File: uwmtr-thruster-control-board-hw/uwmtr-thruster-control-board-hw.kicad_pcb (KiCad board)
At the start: 4 copper layers, 40 x 49.2 mm, 16 parts, among them J1 Conn_01x13_Pin, J2 691137710003, J3 691137710002, U1 TI_MCF8316A

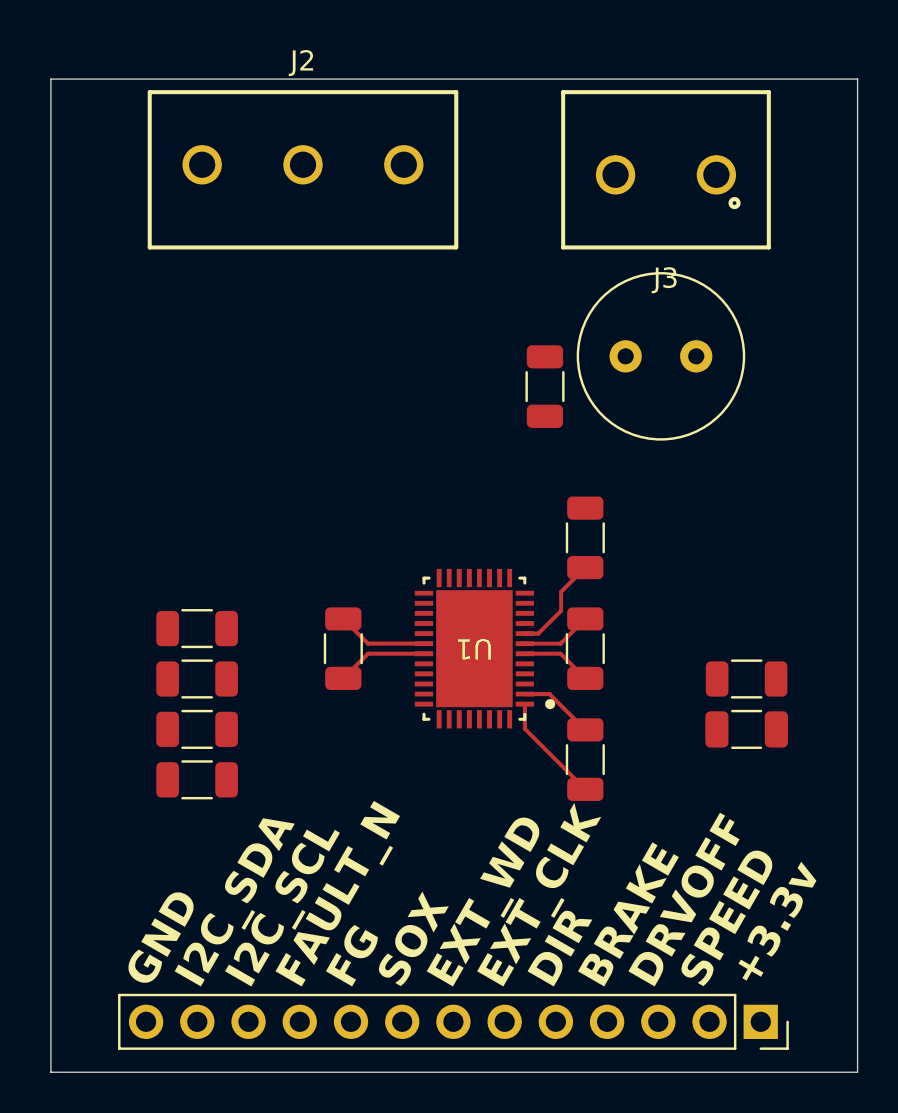
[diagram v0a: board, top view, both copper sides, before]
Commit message: Completing component placement for layout and replacing the resistor
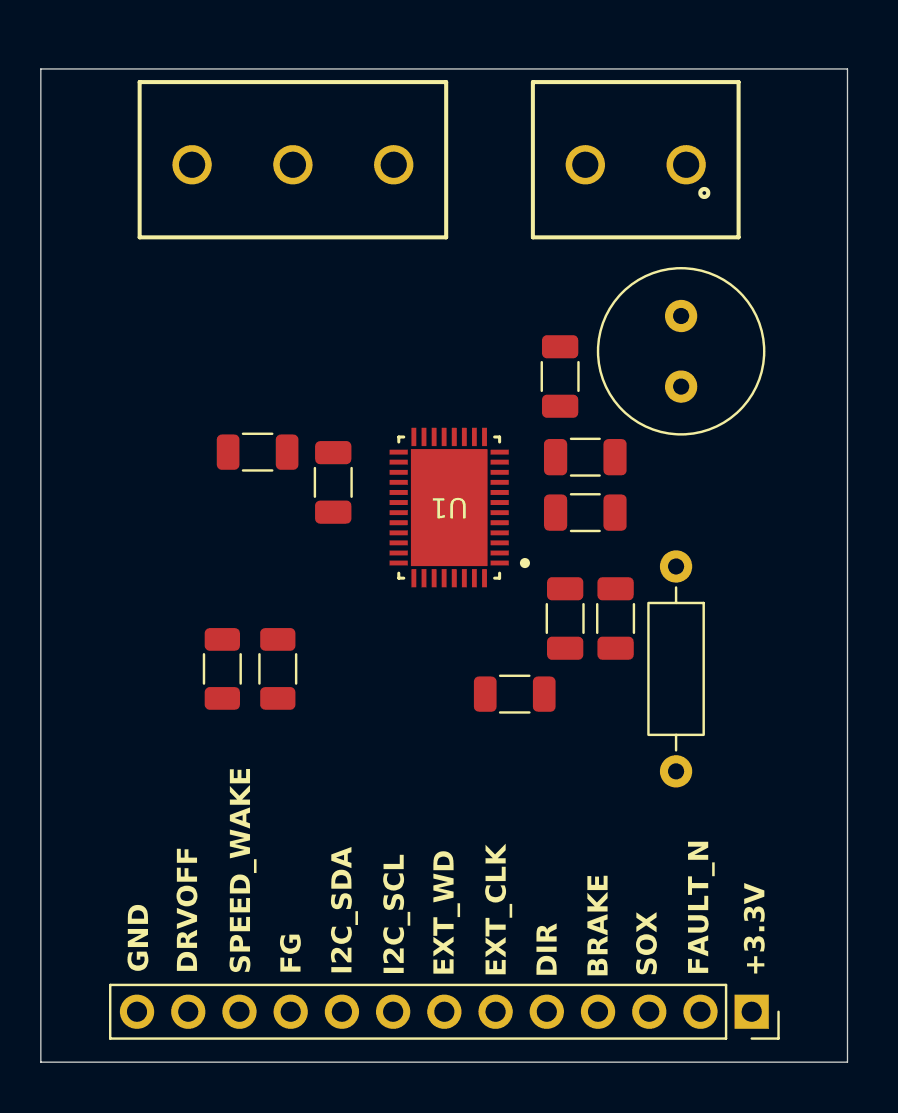
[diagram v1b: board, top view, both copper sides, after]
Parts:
- removed FRC1206F22R0TS1: 22R, Resistor_SMD:R_1206_3216Metric
- added R1: 22Ω, Resistor_THT:R_Axial_DIN0207_L6.3mm_D2.5mm_P10.16mm_Horizontal, F.Cu at (171.5, 109.9)
- moved 1206W4F5101T5E2 16.3 mm to (163.5, 116.2), turned to 0 degrees
- moved 1206W4F5101T5E1 9.25 mm to (150.8, 104.2), turned to 180 degrees
- moved CS3216X5R226K160NRI1 8.51 mm to (168.5, 112.5), turned to -90 degrees
- moved CL31B105KAHNNNE2 8.26 mm to (154.5, 105.8)
- moved U1 7.11 mm to (160.2, 107.0)
- moved CL31B105KAHNNNE3 7.07 mm to (166.0, 112.5)
- moved 1206B473K500NT1 6.75 mm to (167.0, 107.2), turned to 0 degrees
- moved 1206W4F5101T5E3 5.00 mm to (151.8, 115.0), turned to -90 degrees
- moved CL31B105KAHNNNE1 4.00 mm to (167.0, 104.5), turned to 180 degrees
- moved KM107M050F12RR0VH2FP1 1.68 mm to (171.8, 101.0), turned to 90 degrees
- moved J3 1.58 mm to (169.5, 90.0)
- moved 1206W4F5101T5E4 1.35 mm to (149.0, 115.0), turned to -90 degrees
- moved CL31B104KCFNNNE1 0.90 mm to (165.8, 100.5)
- moved J1 0.67 mm to (175.2, 132.0)
- moved J2 0.50 mm to (152.5, 90.0), turned to 180 degrees
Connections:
- 1206W4F5101T5E1 pad 1: +3.3V -> /AVDD
- 1206W4F5101T5E2 pad 2: +3.3V -> /AVDD
- 1206W4F5101T5E3 pad 2: +3.3V -> /AVDD
- 1206W4F5101T5E4 pad 2: +3.3V -> /AVDD
- J1 pad 10: /I2C_SDA -> /FG
- J1 pad 11: /I2C_SCL -> /SPEED_WAKE
- J1 pad 12: /FAULT_N -> /DRVOFF
- J1 pad 13: /SPEED_WAKE -> GND
- J1 pad 2: GND -> /FAULT_N
- J1 pad 3: /DRVOFF -> /SOX
- J1 pad 8: /SOX -> /I2C_SCL
- J1 pad 9: /FG -> /I2C_SDA
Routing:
- net GND: track 8.49 -> 0.00 mm
- net /DVDD: track 5.47 -> 0.00 mm
- net /CP: track 4.90 -> 0.00 mm
- net /AVDD: track 4.76 -> 0.00 mm
- net /CPL: track 3.50 -> 0.00 mm
- net /CPH: track 3.50 -> 0.00 mm
- added copper zone on In1.Cu, net GND
- added copper zone on In2.Cu, net GND
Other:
- board text added: "+3.3V"
- board text added: "SPEED_WAKE"
- board text removed: "+3.3v"
- board text removed: "SPEED"

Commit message: Adding some routes
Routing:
- net /CPL: track 0.00 -> 6.72 mm
- net /CP: track 0.00 -> 4.04 mm
- net /CPH: track 0.00 -> 2.98 mm
- net GND: vias 0 -> 7
- added copper zone on F.Cu, net +24V
- added copper zone on F.Cu, net GND
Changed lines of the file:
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@@
+		)
+	)
+	(segment
+		(start 162.753033 106.75)
+		(end 165.025 106.75)
+		(width 0.2)
+		(layer "F.Cu")
+		(net "/CPH")
+	)
+	(segment
+		(start 165.025 106.75)
+		(end 165.525 107.25)
+		(width 0.2)
+		(layer "F.Cu")
+		(net "/CPH")
+	)
+	(segment
+		(start 163.765256 107.25)
+		(end 164.965256 108.45)
+		(width 0.2)
+		(layer "F.Cu")
+		(net "/CPL")
+	)
+	(segment
+		(start 164.965256 108.45)
+		(end 167.275 108.45)
+		(width 0.2)
+		(layer "F.Cu")
+		(net "/CPL")
+	)
+	(segment
+		(start 162.753033 107.25)
+		(end 163.765256 107.25)
+		(width 0.2)
+		(layer "F.Cu")
+		(net "/CPL")
+	)
+	(segment
+		(start 167.275 108.45)
+		(end 168.475 107.25)
+		(width 0.2)
+		(layer "F.Cu")
+		(net "/CPL")
+	)
+	(via
+		(at 173.85 98.7)
+		(size 0.6)
+		(drill 0.3)
+		(layers "F.Cu" "B.Cu")
+		(free yes)
+		(net "GND")
+	)
+	(via
+		(at 167.15 97)
+		(size 0.6)
+		(drill 0.3)
+		(layers "F.Cu" "B.Cu")
+		(free yes)
+		(net "GND")
+	)
+	(via
+		(at 169.85 98.75)
+		(size 0.6)
+		(drill 0.3)
+		(layers "F.Cu" "B.Cu")
+		(free yes)
+		(net "GND")
+	)
+	(via
+		(at 169.7 95.9)
+		(size 0.6)
+		(drill 0.3)
+		(layers "F.Cu" "B.Cu")
+		(free yes)
+		(net "GND")
+	)
+	(via
+		(at 163.95 96.95)
+		(size 0.6)
+		(drill 0.3)
+		(layers "F.Cu" "B.Cu")
+		(free yes)
+		(net "GND")
+	)
+	(via
+		(at 163 103.3)
+		(size 0.6)
+		(drill 0.3)
+		(layers "F.Cu" "B.Cu")
+		(free yes)
+		(net "GND")
+	)
+	(via
+		(at 173.6 95.95)
+		(size 0.6)
+		(drill 0.3)
+		(layers "F.Cu" "B.Cu")
+		(free yes)
+		(net "GND")
+	)
+	(segment
+		(start 162.753033 106.249999)
+		(end 164.700001 106.249999)
+		(width 0.2)
+		(layer "F.Cu")
+		(net "/CP")
+	)
+	(segment
+		(start 164.700001 106.249999)
+		(end 165.525 105.425)
+		(width 0.2)
+		(layer "F.Cu")
+		(net "/CP")
+	)
+	(segment
+		(start 165.525 105.425)
+		(end 165.525 104.5)
+		(width 0.2)
+		(layer "F.Cu")
+		(net "/CP")
+	)
+	(zone
+		(net "+24V")
+		(layer "F.Cu")
+		(hatch edge 0.5)
+		(priority 3)
+		(connect_pads thru_hole_only
+			(clearance 0.25)
+		)
+		(min_thickness 0.25)
+		(fill yes
+			(thermal_gap 0.5)
+			(thermal_bridge_width 0.5)
+			(island_removal_mode 1)
+		)
+		(polygon
+			(pts
+				(xy 162.3 104.65) (xy 163.55 104.65) (xy 163.55 100.55) (xy 168.5 100.55) (xy 168.5 103.35) (xy 164.7 103.35)
+				(xy 164.7 105.9) (xy 162.3 105.9)
+			)
 		)
 	)
 	(zone
 		(net "GND")
+		(layer "F.Cu")
+		(hatch edge 0.5)
+		(priority 2)
+		(connect_pads thru_hole_only
+			(clearance 0.25)
+		)
+		(min_thickness 0.25)
+		(fill yes
+			(thermal_gap 0.5)
+			(thermal_bridge_width 0.5)
+			(island_removal_mode 1)
+		)
+		(polygon
+			(pts
+				(xy 162.5 104.35) (xy 163.5 104.35) (xy 163.5 100.5) (xy 168.5 100.5) (xy 169.7 99.3) (xy 175.5 99.3)
+				(xy 175.5 95) (xy 162.5 95)
+			)
+		)
+	)
+	(zone
+		(net "+24V")
+		(layer "F.Cu")
+		(hatch edge 0.5)
+		(priority 4)
+		(connect_pads thru_hole_only
+			(clearance 0.25)
+		)
+		(min_thickness 0.25)
+		(fill yes
+			(thermal_gap 0.5)
+			(thermal_bridge_width 0.5)
+			(island_removal_mode 1)
+		)
+		(polygon
+			(pts
+				(xy 168.5 100.55) (xy 169.655 99.45) (xy 175.5 99.45) (xy 175.5 105.75) (xy 167 105.9) (xy 167 100.55)
+			)
+		)
+	)
+	(zone
+		(net "GND")

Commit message: Adding routing for OUT_A, OUT_B and OUT_C
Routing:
- net GND: vias 7 -> 17
- added copper zone on B.Cu, net +24V
- added copper zone on B.Cu, net /OUT_A
- added copper zone on F.Cu, net /OUT_A
- added copper zone on B.Cu, net /OUT_B
- added copper zone on F.Cu, net /OUT_B
- added copper zone on B.Cu, net /OUT_C
- added copper zone on F.Cu, net /OUT_C
- added copper zone on B.Cu, net GND

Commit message: Completing layout
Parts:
- added G***: LOGO, LOGO, F.Cu at (144.0, 97.3)
- moved R1 1.12 mm to (172.5, 109.4)
- moved 1206W4F5101T5E4 0.75 mm to (148.2, 115.0)
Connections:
- CL31B104KCFNNNE1 pad 1: GND -> PGND
- CL31B105KAHNNNE2 pad 1: GND -> AGND
- CL31B105KAHNNNE3 pad 1: GND -> AGND
- CS3216X5R226K160NRI1 pad 2: GND -> AGND
- J1 pad 13: GND -> AGND
- J3 pad 2: GND -> PGND
- KM107M050F12RR0VH2FP1 pad 2: GND -> PGND
- U1 pad 12: GND -> PGND
- U1 pad 15: GND -> PGND
- U1 pad 18: GND -> PGND
- U1 pad 2: GND -> AGND
- U1 pad 26: GND -> AGND
- U1 pad 4: GND -> AGND
- U1 pad 41: GND -> AGND
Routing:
- net /AVDD: track 0.00 -> 45.0 mm, vias 0 -> 5
- net /FG: track 0.00 -> 43.3 mm
- net /I2C_SDA: track 0.00 -> 35.3 mm
- net /DRVOFF: track 0.00 -> 35.0 mm, vias 0 -> 1
- net /I2C_SCL: track 0.00 -> 31.0 mm
- net /SPEED_WAKE: track 0.00 -> 28.5 mm, vias 0 -> 1
- net /EXT_WD: track 0.00 -> 27.0 mm
- net /FAULT_N: track 0.00 -> 25.9 mm
- net /EXT_CLK: track 0.00 -> 25.5 mm
- net /SOX: track 0.00 -> 25.3 mm
- net /DIR: track 0.00 -> 25.1 mm
- net /BRAKE: track 0.00 -> 24.9 mm
- net +3.3V: track 0.00 -> 6.70 mm
- net /SW_BK: track 0.00 -> 3.47 mm
- net PGND: vias 0 -> 8
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- added copper zone on F.Cu, net +3.3V
- added copper zone on F.Cu, net /DVDD
- added copper zone on F.Cu, net /SW_BK
- added copper zone on F.Cu, net AGND
- added copper zone on In1.Cu, net AGND
- added copper zone on In2.Cu, net AGND
- added copper zone on B.Cu, net PGND
- added copper zone on F.Cu, net PGND
- added copper zone on In1.Cu, net PGND
- added copper zone on In2.Cu, net PGND
- removed copper zone on B.Cu, net GND
- removed copper zone on F.Cu, net GND
- removed copper zone on In1.Cu, net GND
- removed copper zone on In2.Cu, net GND
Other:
- board text added: "GitHub: AdrianTarantino"
- board text added: "UWMTR - MCF8316A Eval Board"

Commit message: Adding more labels.
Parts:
- moved KM107M050F12RR0VH2FP1 1.17 mm to (172.5, 101.9)
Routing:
- net +24V: vias 9 -> 8
- added copper zone on B.Cu, net +3.3V
- added copper zone on B.Cu, net /SW_BK
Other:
- board text added: "+24V"
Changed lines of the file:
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@@
 	(footprint "Capacitor_THT:C_Radial_D8.0mm_H11.5mm_P3.50mm"
 		(layer "F.Cu")
-		(at 171.75 101 90)
+		(at 172.5 101.9 90)
 		(descr "C, Radial series, Radial, pin pitch=3.50mm, diameter=8mm, height=11.5mm, Non-Polar Electrolytic Capacitor")
 		(tags "C Radial series Radial pin pitch 3.50mm diameter 8mm height 11.5mm Non-Polar Electrolytic Capacitor")
@@
 		(layer "Edge.Cuts")
 	)
+	(gr_text "GND"
+		(at 168.5 94 180)
+		(layer "F.SilkS")
+		(effects
+			(font
+				(size 1 1)
+				(thickness 0.1)
+			)
+			(justify left bottom)
+		)
+	)
+	(gr_text "+24V"
+		(at 174.4 94 180)
+		(layer "F.SilkS")
+		(effects
+			(font
+				(size 1 1)
+				(thickness 0.1)
+			)
+			(justify left bottom)
+		)
+	)
 	(gr_text "GitHub: AdrianTarantino"
 		(at 142.3 99.9 270)
@@
 	)
 	(gr_text "GND"
-		(at 145.43603 130.043163 90)
+		(at 144.18603 127 270)
 		(layer "F.SilkS")
 		(effects
@@
 	)
 	(gr_text "DRVOFF"
-		(at 147.86837 130.1 90)
+		(at 146.58281 124.591036 270)
 		(layer "F.SilkS")
 		(effects
@@
 	)
 	(gr_text "SPEED_WAKE"
-		(at 150.495301 130.127398 90)
+		(at 149.25 120.870802 270)
 		(layer "F.SilkS")
 		(effects
@@
 	)
 	(gr_text "FG"
-		(at 152.998815 130.137985 90)
+		(at 151.748815 128.387985 270)
 		(layer "F.SilkS")
 		(effects
@@
 	)
 	(gr_text "I2C_SDA"
-		(at 155.52563 130.169515 90)
+		(at 154.25 124.169515 270)
 		(layer "F.SilkS")
 		(effects
@@
 	)
 	(gr_text "I2C_SCL"
-		(at 158.115969 130.205195 90)
+		(at 156.71 124.17 270)
 		(layer "F.SilkS")
 		(effects
@@
 	)
 	(gr_text "EXT_WD"
-		(at 160.587837 130.236841 90)
+		(at 159.337837 124.736841 270)
 		(layer "F.SilkS")
 		(effects
@@
 	)
 	(gr_text "EXT_CLK"
-		(at 163.17265 130.268371 90)
+		(at 161.92265 124 270)
 		(layer "F.SilkS")
 		(effects
@@
 	)
 	(gr_text "DIR"
-		(at 165.699697 130.294839 90)
+		(at 164.40468 127.746989 270)
 		(layer "F.SilkS")
 		(effects
@@
 	)
 	(gr_text "BRAKE"
-		(at 168.22427 130.318603 90)
+		(at 166.97427 125.568603 270)
 		(layer "F.SilkS")
 		(effects
@@
 	)
 	(gr_text "SOX"
-		(at 170.654021 130.24225 90)
+		(at 169.404021 127.24225 270)
 		(layer "F.SilkS")
 		(effects
@@
 	)
 	(gr_text "FAULT_N"
-		(at 173.215186 130.200133 90)
+		(at 172.131402 124.148193 270)
 		(layer "F.SilkS")
 		(effects
@@
 	)
 	(gr_text "+3.3V"
-		(at 176 130.25 90)
+		(at 174.452806 125.677959 270)
 		(layer "F.SilkS")
 		(effects
@@
 	)
 	(via
-		(at 174 102.5)
-		(size 0.6)
-		(drill 0.3)
-		(layers "F.Cu" "B.Cu")
-		(free yes)
-		(net "+24V")
-	)
-	(via
 		(at 172 93.5)
 		(size 0.6)
@@
 	)
 	(zone
-		(net "+3.3V")
-		(layer "F.Cu")
-		(hatch edge 0.5)
-		(priority 21)
-		(connect_pads thru_hole_only
-			(clearance 0.1)
-		)
-		(min_thickness 0.25)
-		(fill yes
-			(thermal_gap 0.5)
-			(thermal_bridge_width 0.5)
-			(island_removal_mode 1)
-		)
-		(polygon
-			(pts
-				(xy 167.5 110) (xy 167.5 112) (xy 168.25 112) (xy 170.25 114) (xy 170.25 121.5) (xy 179.5 121.5)
-				(xy 179.5 113.5) (xy 173.85 113.5) (xy 170 110)
-			)
-		)
-	)
-	(zone
 		(net "AGND")
 		(layer "F.Cu")
@@
 	)
 	(zone
-		(net "+3.3V")
-		(layer "F.Cu")
-		(hatch edge 0.5)
-		(priority 22)
-		(connect_pads thru_hole_only
-			(clearance 0.1)
-		)
-		(min_thickness 0.25)
-		(fill yes
-			(thermal_gap 0.5)
-			(thermal_bridge_width 0.5)
-			(island_removal_mode 1)
-		)
-		(polygon
-			(pts
-				(xy 174 134.4) (xy 174 121.25) (xy 179.5 121.25) (xy 179.5 134.4)
-			)
-		)
-	)
-	(zone
 		(net "PGND")
 		(layer "F.Cu")
@@
 	)
 	(zone
-		(net "/SW_BK")
-		(layer "F.Cu")
-		(hatch edge 0.5)
-		(priority 16)
-		(connect_pads thru_hole_only
-			(clearance 0.1)
-		)
-		(min_thickness 0.25)
-		(fill yes
-			(thermal_gap 0.5)
-			(thermal_bridge_width 0.5)
-			(island_removal_mode 1)
-		)
-		(polygon
-			(pts
-				(xy 164.5 109) (xy 169.5 109) (xy 169.5 106) (xy 179.5 106) (xy 179.5 113.5) (xy 173.85 113.5) (xy 170 110)
-				(xy 164.5 110)
-			)
-		)
-	)
-	(zone
 		(net "AGND")
 		(layer "F.Cu")
@@
 		(polygon
 			(pts
-				(xy 162.3 104.65) (xy 163.55 104.65) (xy 163.55 100.55) (xy 168.5 100.55) (xy 168.5 103.35) (xy 164.7 103.35)
+				(xy 162.3 104.65) (xy 163.55 104.65) (xy 163.55 100.3) (xy 179.5 100.3) (xy 179.5 103.35) (xy 164.7 103.35)
 				(xy 164.7 105.9) (xy 162.3 105.9)
 			)
@@
 	)
 	(zone
+		(net "+3.3V")
+		(layers "F.Cu" "B.Cu")
+		(hatch edge 0.5)
+		(priority 21)
+		(connect_pads thru_hole_only
+			(clearance 0.1)
+		)
+		(min_thickness 0.25)
+		(fill yes
+			(thermal_gap 0.5)
+			(thermal_bridge_width 0.5)
+			(island_removal_mode 1)
+		)
+		(polygon
+			(pts
+				(xy 167.5 110) (xy 167.5 112) (xy 168.25 112) (xy 170.25 114) (xy 170.25 121.5) (xy 179.5 121.5)
+				(xy 179.5 113.5) (xy 173.85 113.5) (xy 170 110)
+			)
+		)
+	)
+	(zone
 		(net "/OUT_A")
 		(layers "F.Cu" "B.Cu")
@@
 		(polygon
 			(pts
-				(xy 162.5 104.35) (xy 163.5 104.35) (xy 163.5 100.5) (xy 168.5 100.5) (xy 169.7 99.3) (xy 175.5 99.3)
+				(xy 162.5 104.35) (xy 163.5 104.35) (xy 163.5 100.5) (xy 168.5 100.5) (xy 168.947744 100.4) (xy 175.395 100.45)
 				(xy 175.5 95) (xy 162.5 95)
 			)
@@
 	)
 	(zone
+		(net "+3.3V")
+		(layers "F.Cu" "B.Cu")
+		(hatch edge 0.5)
+		(priority 22)
+		(connect_pads thru_hole_only
+			(clearance 0.1)
+		)
+		(min_thickness 0.25)
+		(fill yes
+			(thermal_gap 0.5)
+			(thermal_bridge_width 0.5)
+			(island_removal_mode 1)
+		)
+		(polygon
+			(pts
+				(xy 174 134.4) (xy 174 121.25) (xy 179.5 121.25) (xy 179.5 134.4)
+			)
+		)
+	)
+	(zone
 		(net "/OUT_C")
 		(layers "F.Cu" "B.Cu")
@@
 	)
 	(zone
-		(net "/OUT_B")
+		(net "/SW_BK")
 		(layers "F.Cu" "B.Cu")
 		(hatch edge 0.5)
-		(priority 10)
+		(priority 16)
 		(connect_pads thru_hole_only
 			(clearance 0.1)
@@
 		(polygon
 			(pts
-				(xy 160.625 103.95) (xy 159.9 103.95) (xy 159.9 95.5) (xy 150.55 95.5) (xy 150.55 85.811023) (xy 154.575 85.825)
-				(xy 154.575 94.225) (xy 160.625 94.225)
+				(xy 164.5 109) (xy 169.5 109) (xy 169.5 106) (xy 179.5 106) (xy 179.5 113.5) (xy 173.85 113.5) (xy 170 110)
+				(xy 164.5 110)
 			)
 		)
@@
 		(priority 7)
 		(connect_pads thru_hole_only
-			(clearance 0.25)
+			(clearance 0.15)
+		)
+		(min_thickness 0.25)
+		(fill yes
+			(thermal_gap 0.5)
+			(thermal_bridge_width 0.5)
+			(island_removal_mode 1)
+		)
+		(polygon
+			(pts
+				(xy 175.5 103.1) (xy 175.5 106) (xy 167 106) (xy 167 103.1)
+			)
+		)
+	)
+	(zone
+		(net "/OUT_B")
+		(layers "F.Cu" "B.Cu")
+		(hatch edge 0.5)
+		(priority 10)
+		(connect_pads thru_hole_only
+			(clearance 0.1)
 		)
 		(min_thickness 0.25)
@@
 		(polygon
 			(pts
-				(xy 168.5 100.55) (xy 169.655 99.45) (xy 175.5 99.45) (xy 175.5 105.75) (xy 167 105.9) (xy 167 100.55)
+				(xy 160.625 103.95) (xy 159.9 103.95) (xy 159.9 95.5) (xy 150.55 95.5) (xy 150.55 85.811023) (xy 154.575 85.825)
+				(xy 154.575 94.225) (xy 160.625 94.225)
 			)
 		)
